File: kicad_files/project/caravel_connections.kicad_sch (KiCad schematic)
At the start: 9 parts, among them U1 Caravel_WCSP, U3 caravel-M.2-card

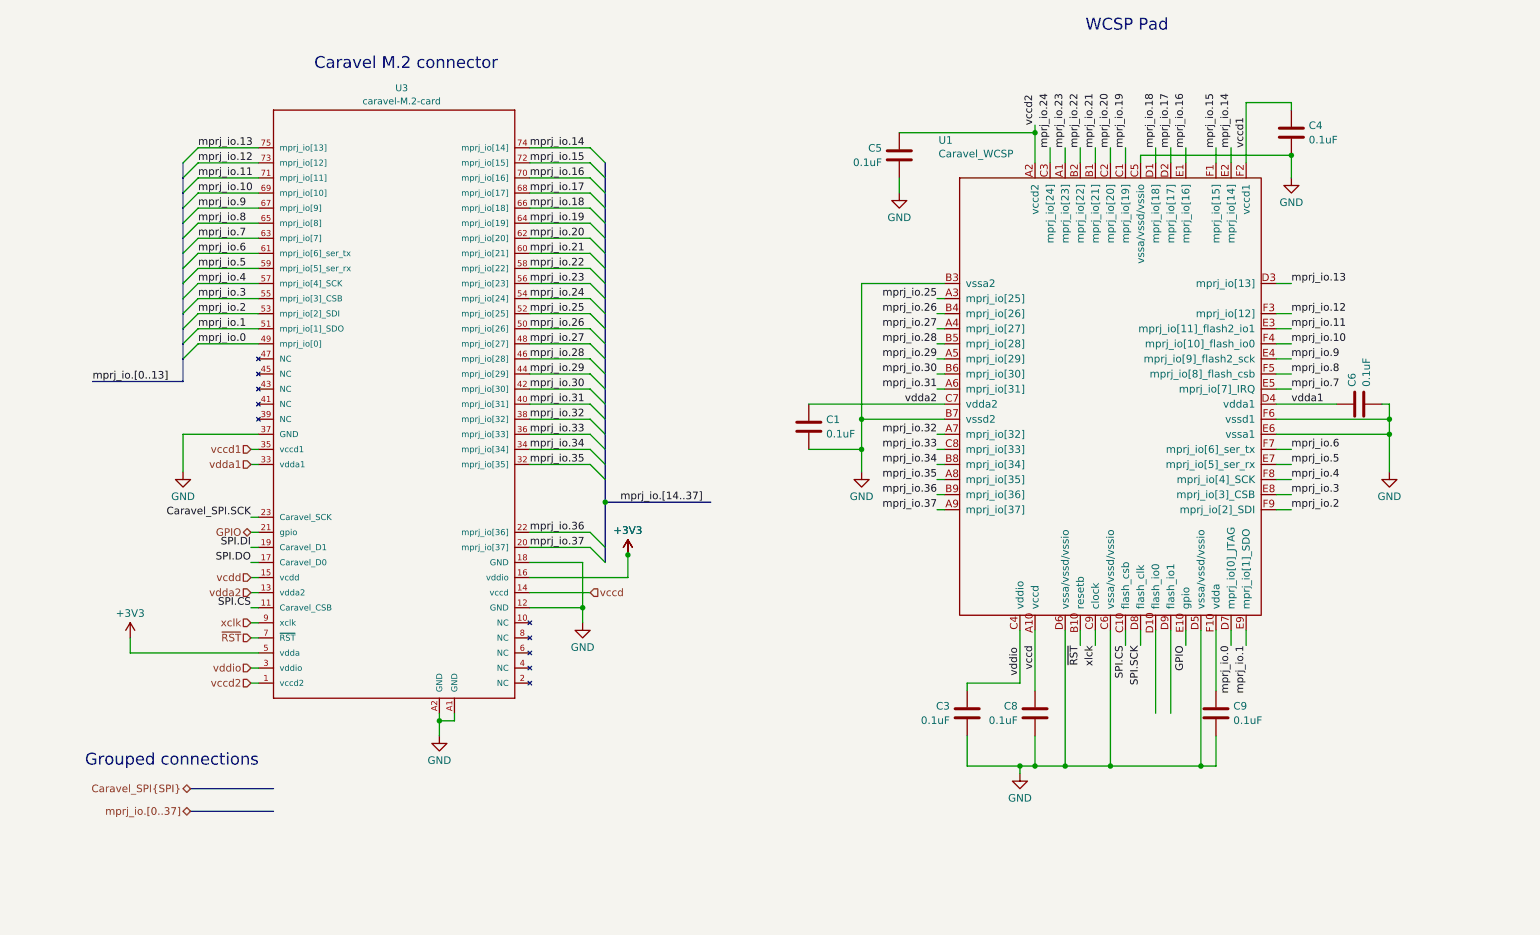
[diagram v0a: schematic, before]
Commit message: feat: schematic almost done, also add all footprints and symbol libraries except for external libraries
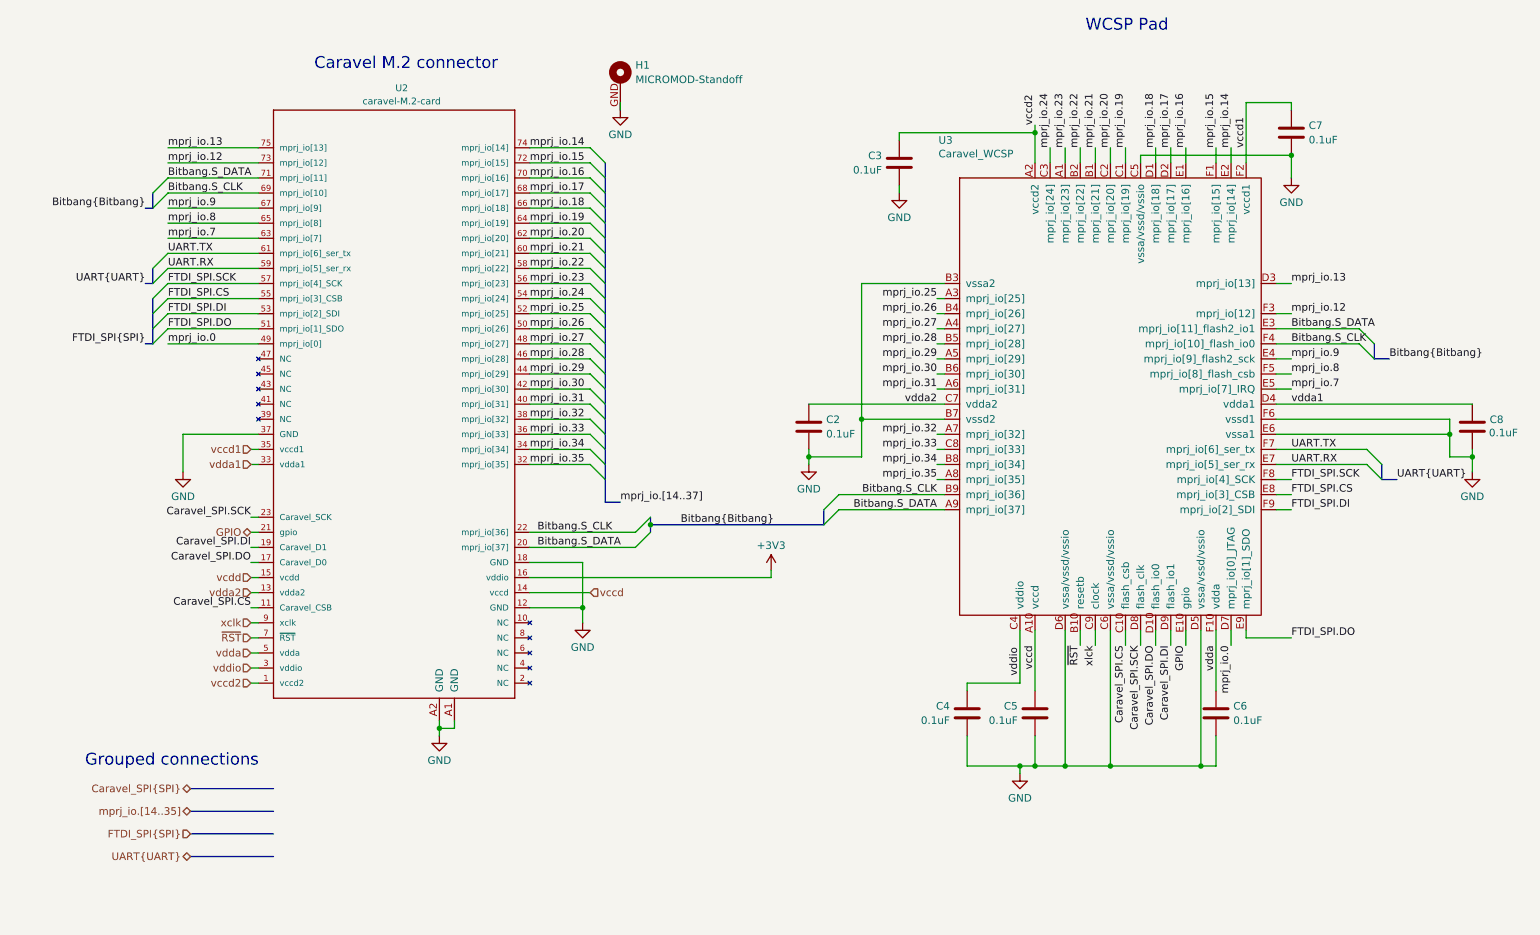
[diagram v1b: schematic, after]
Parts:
- added H1: MICROMOD-Standoff, MicroMod-Sparkfun:MicroMod-Standoff, symbol MicroMod-Sparkfun:MICROMOD-Standoff
- U2: renamed from U3; footprint (none) -> MicroMod-Sparkfun:M.2-CONNECTOR-E
- renumbered C1 to C2, C5 to C3, C3 to C4, C8 to C5, C9 to C6, C4 to C7, C6 to C8, U1 to U3
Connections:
- net SPI.DI is gone; now on net Caravel_SPI.DI: U2.19 (Caravel_D1)
- net SPI.DO is gone; now on net Caravel_SPI.DO: U2.17 (Caravel_D0)
- net SPI.SCK is gone; now on net Caravel_SPI.SCK: U3.D8 (flash_clk)
- net mprj_io.36 is gone; now on net Bitbang.S_CLK: U2.22 (mprj_io[36]), U3.B9 (mprj_io[36])
- net mprj_io.37 is gone; now on net Bitbang.S_DATA: U2.20 (mprj_io[37]), U3.A9 (mprj_io[37])
- net +3V3: no longer U2.5 (vdda)
- net GND: now also H1.GND
- net Caravel_SPI.DO: now reaches U3.D10 (flash_io0)
- net Caravel_SPI.DI: now reaches U3.D9 (flash_io1)
- net vdda: now reaches C6.1, U3.F10 (vdda)
- net vdda: now also U2.5 (vdda)
- net SPI.CS renamed Caravel_SPI.CS
- net mprj_io.1 renamed FTDI_SPI.DO
- net mprj_io.10 renamed Bitbang.S_CLK
- net mprj_io.11 renamed Bitbang.S_DATA
- net mprj_io.2 renamed FTDI_SPI.DI
- net mprj_io.3 renamed FTDI_SPI.CS
- net mprj_io.4 renamed FTDI_SPI.SCK
- net mprj_io.5 renamed UART.RX
- net mprj_io.6 renamed UART.TX
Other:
- moved on the sheet: C3, C8, U2

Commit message: started with board layout, also added more stuff on the schematic
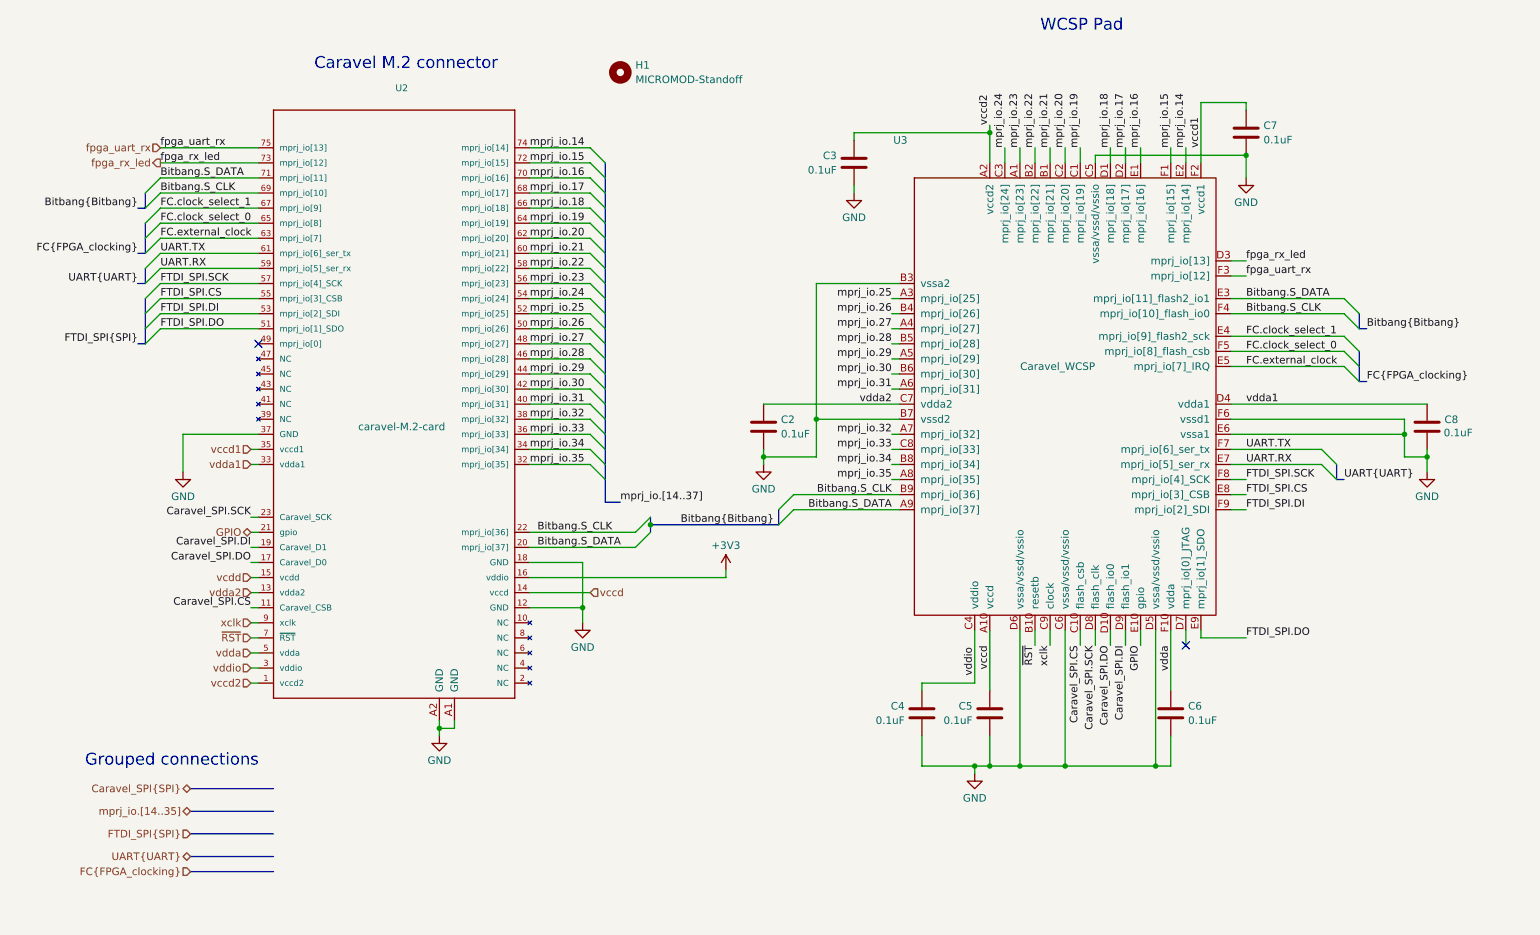
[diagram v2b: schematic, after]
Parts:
- U2: value caravel-M.2-card -> ~
- U3: value Caravel_WCSP -> ~
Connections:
- net xlck is gone; now on net xclk: U3.C9 (clock)
- net GND: no longer H1.GND
- net mprj_io.0: no longer names the net of U3.D7 (mprj_io[0]_JTAG)
- net mprj_io.0: no longer U2.49 (mprj_io[0])
- net mprj_io.12 renamed fpga_rx_led
- net fpga_rx_led: now also U3.D3 (mprj_io[13]); no longer U3.F3 (mprj_io[12])
- net mprj_io.13 renamed fpga_uart_rx
- net fpga_uart_rx: now also U3.F3 (mprj_io[12]); no longer U3.D3 (mprj_io[13])
- net mprj_io.7 renamed FC.external_clock
- net mprj_io.8 renamed FC.clock_select_0
- net mprj_io.9 renamed FC.clock_select_1
- no-connect marks 0 -> 2
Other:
- moved on the sheet: C2, C3, C4, C5, C6, C7, C8, U3

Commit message: new layout, add more pin header, change the caravel power pin supply
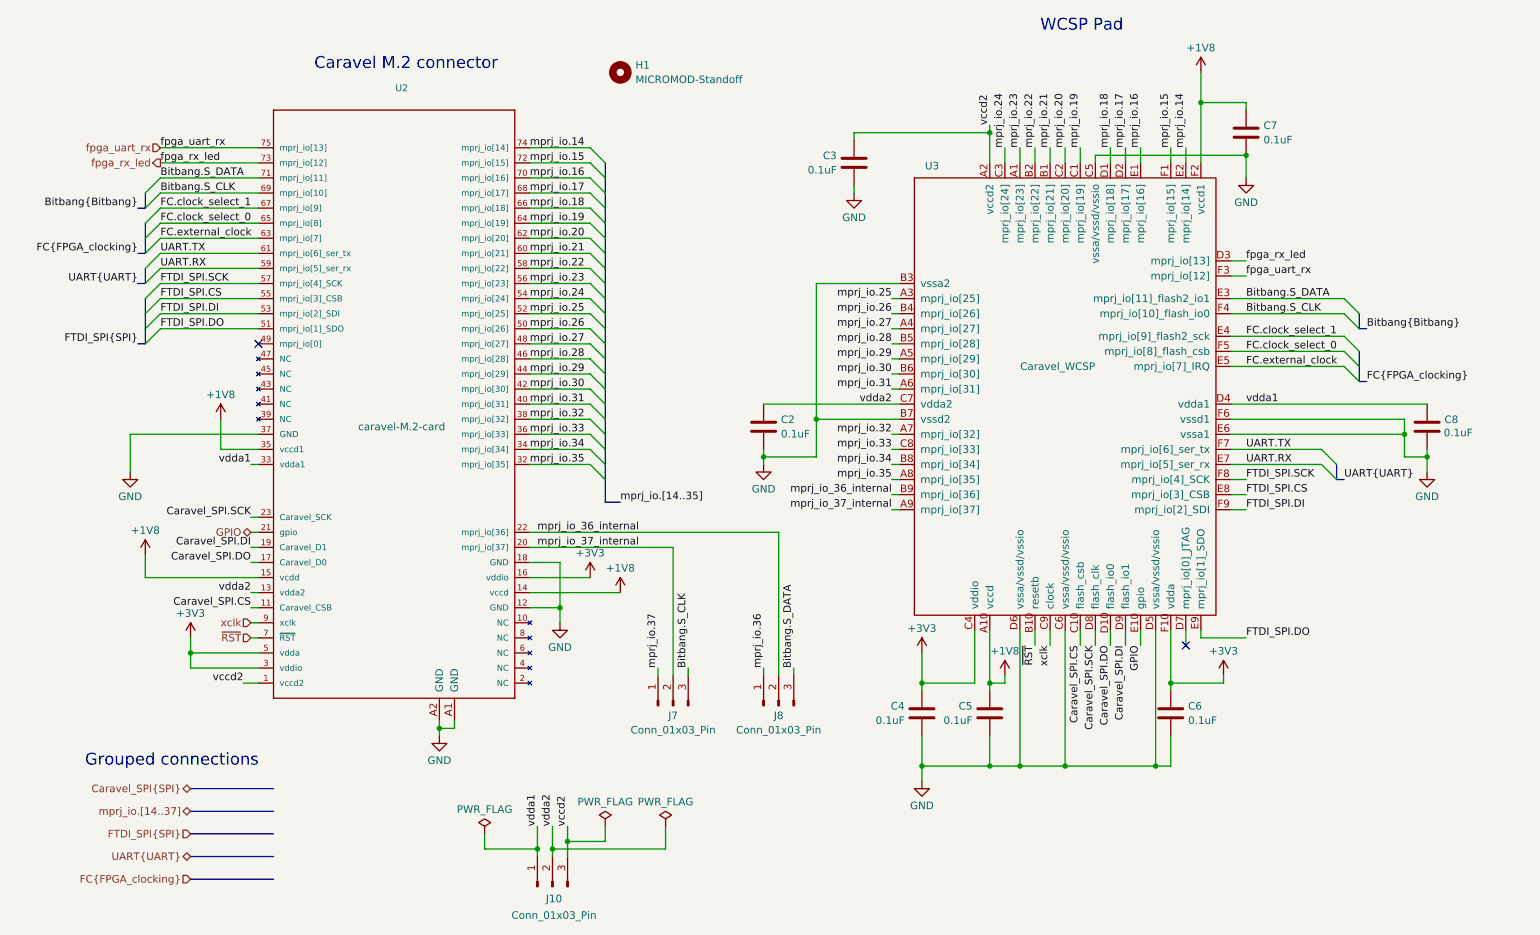
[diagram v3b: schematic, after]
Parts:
- added J10, J7, J8: Conn_01x03_Pin, Connector_PinHeader_2.54mm:PinHeader_1x03_P2.54mm_Vertical, symbol Connector:Conn_01x03_Pin
- U3: footprint Caravel_Board:Caravel_WCSP -> Caravel_Board:Caravel_WCSP_0_25_mm_bga
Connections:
- net vccd1 is gone; now on net +1V8: C7.1, U2.35 (vccd1), U3.F2 (vccd1)
- net vcdd is gone; now on net +1V8: U2.15 (vcdd)
- net vdda is gone; now on net +3V3: C6.1, U2.5 (vdda), U3.F10 (vdda)
- net vddio is gone; now on net +3V3: C4.2, U2.3 (vddio), U3.C4 (vddio)
- net Bitbang.S_CLK: now also J7.3 (Pin_3); no longer U2.22 (mprj_io[36]), U3.B9 (mprj_io[36])
- net Bitbang.S_DATA: now also J8.3 (Pin_3); no longer U2.20 (mprj_io[37]), U3.A9 (mprj_io[37])
- net vccd2: now also J10.3 (Pin_3)
- net vdda1: now also J10.1 (Pin_1)
- net vdda2: now also J10.2 (Pin_2)
- net vccd renamed +1V8
- new net mprj_io.36: J8.1 (Pin_1)
- new net mprj_io.37: J7.1 (Pin_1)
- new net mprj_io_36_internal: J8.2 (Pin_2), U2.22 (mprj_io[36]), U3.B9 (mprj_io[36])
- new net mprj_io_37_internal: J7.2 (Pin_2), U2.20 (mprj_io[37]), U3.A9 (mprj_io[37])
